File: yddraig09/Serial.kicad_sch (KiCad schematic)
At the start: 22 parts, among them J7 Serial 1, J8 Serial 2, Q2 2N4403, Q3 2N4403, U37 SC26C92C1A, U38 MAX208, Y4 3.6864Mhz

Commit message: Updated yddraig09 silkscreen
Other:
- title: Y Ddraig Fechan -> Y Ddraig Fach
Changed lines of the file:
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@@
   (paper "A4")
   (title_block
-    (title "Y Ddraig Fechan")
+    (title "Y Ddraig Fach")
     (company "Stephen Moody")
   )

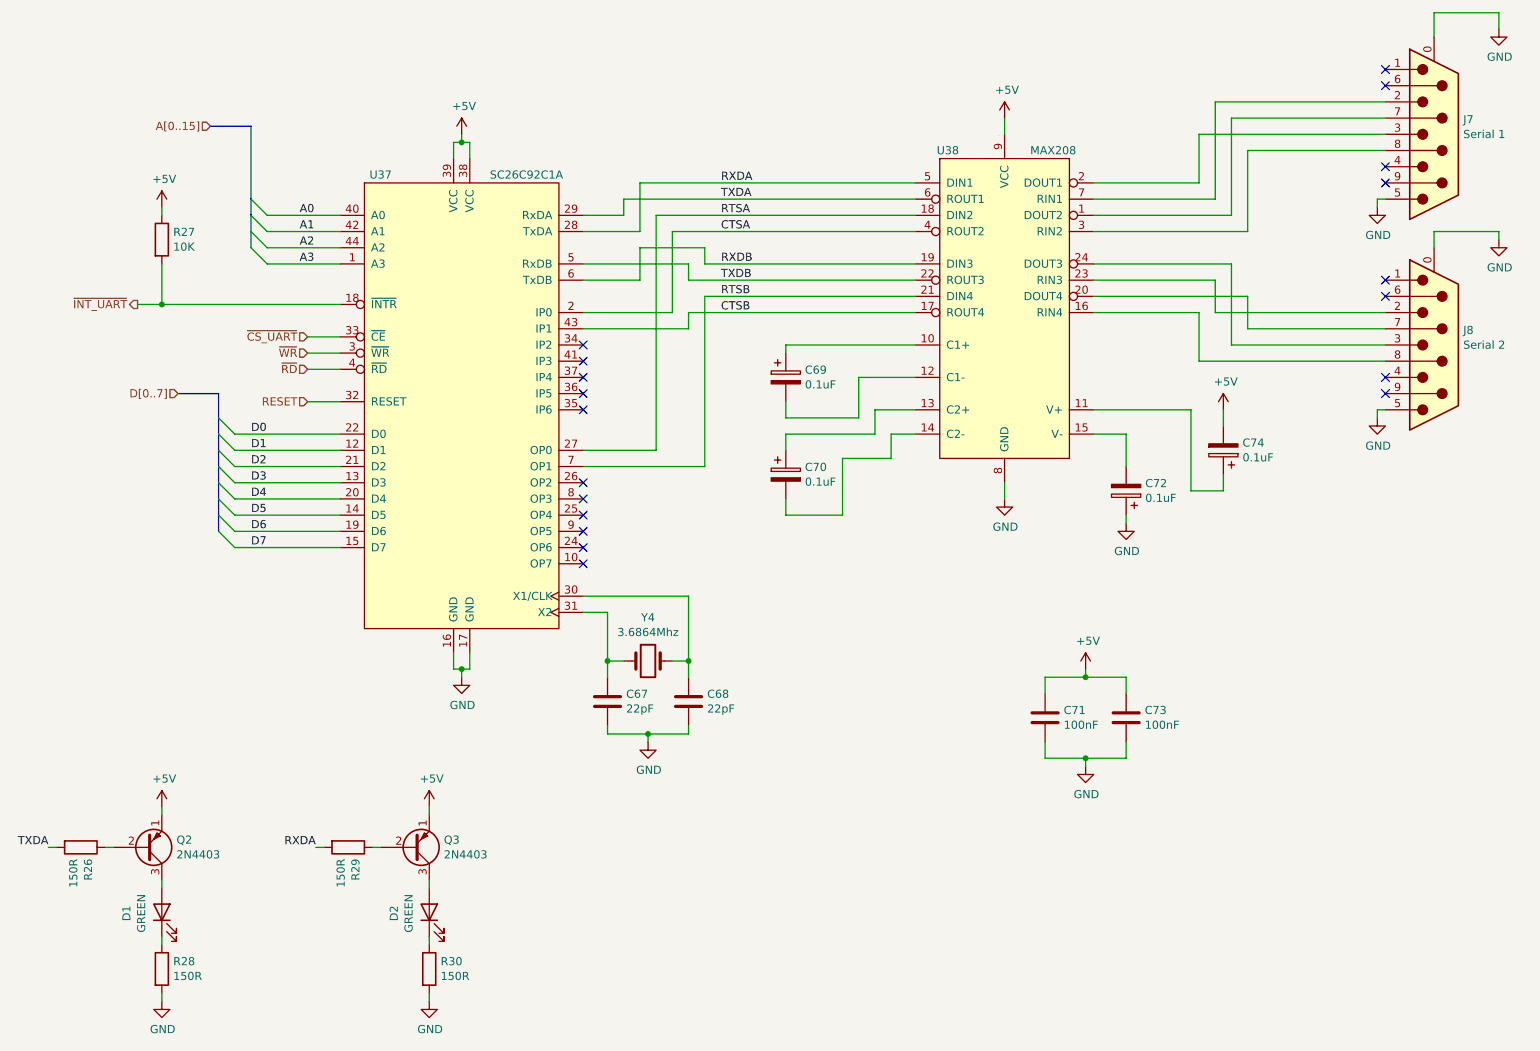
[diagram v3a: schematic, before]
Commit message: Small updates to 6809 and 030 board, remove old files
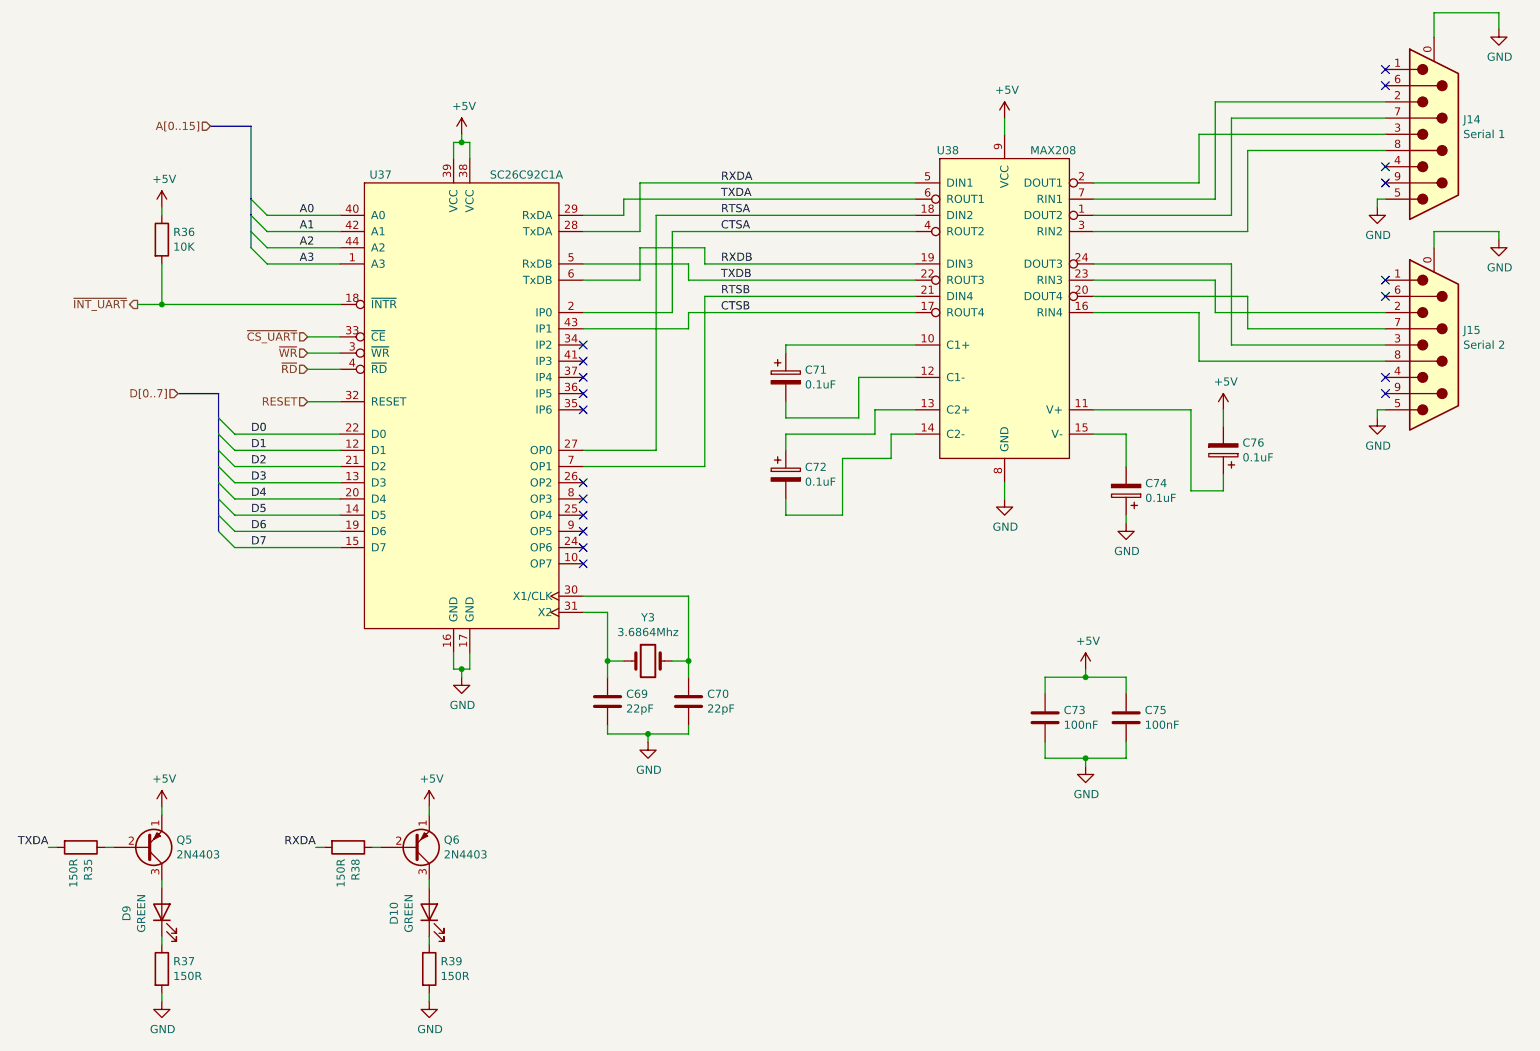
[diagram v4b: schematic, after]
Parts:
- J14: renamed from J7; symbol Connector:DB9_Male_MountingHoles -> Connector:DE9_Plug_MountingHoles
- J15: renamed from J8; symbol Connector:DB9_Male_MountingHoles -> Connector:DE9_Plug_MountingHoles
- renumbered C67 to C69, C68 to C70, C69 to C71, C70 to C72, C71 to C73, C72 to C74, C73 to C75, C74 to C76, D2 to D10, D1 to D9, Q2 to Q5, Q3 to Q6, R26 to R35, R27 to R36, R28 to R37, R29 to R38, R30 to R39, Y4 to Y3

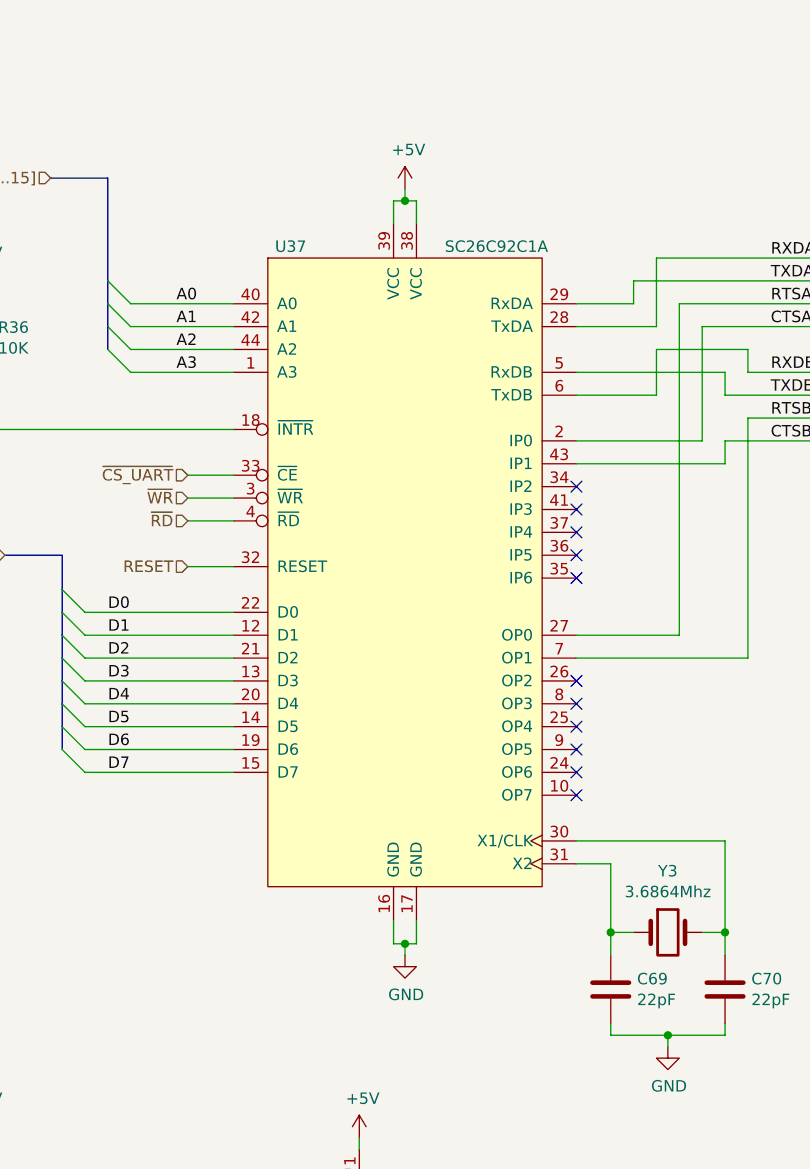
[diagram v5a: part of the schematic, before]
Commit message: Fix the serial port on yddraig09
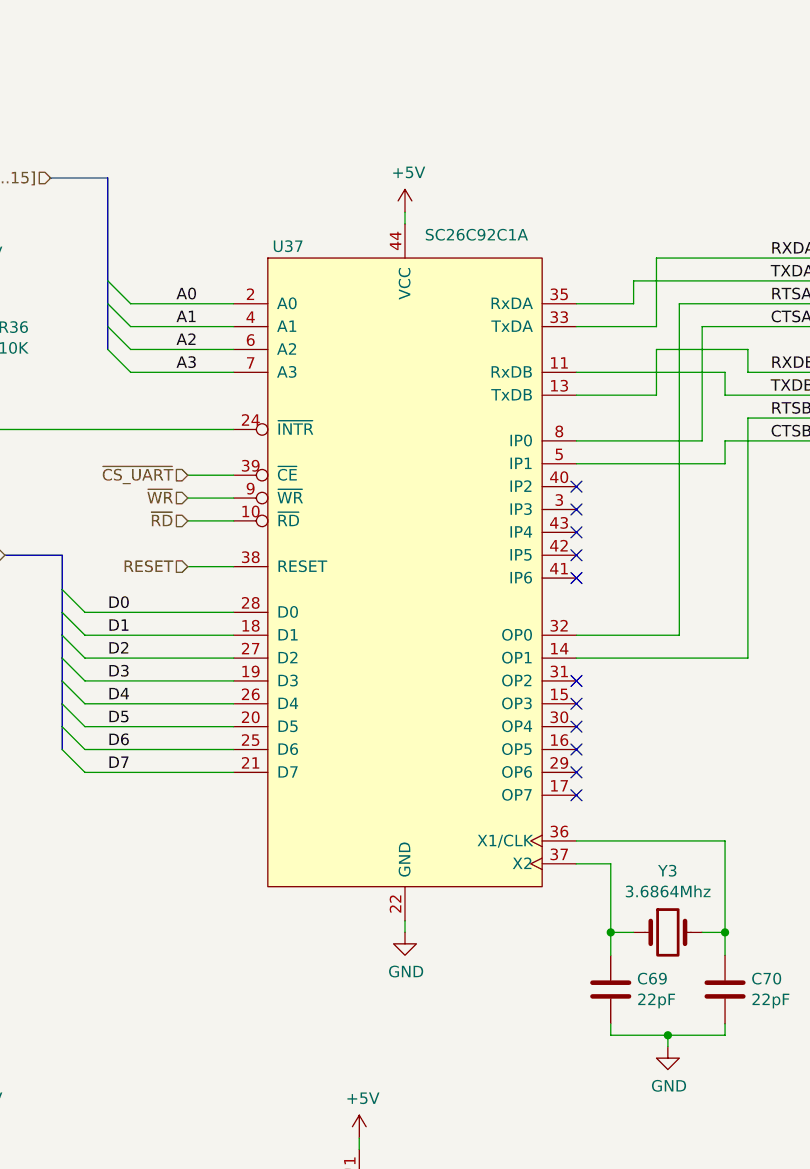
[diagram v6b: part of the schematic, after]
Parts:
- removed U37: SC26C92C1A, Package_LCC:PLCC-44_THT-Socket, symbol Ddraig:SC26C92C1A
- added U37: SC26C92C1A, Package_LCC:PLCC-44_THT-Socket, symbol Ddraig:SC26C92C1A_PLCC
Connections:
- net +5V: now also U37.44 (VCC)
- net A0: now also U37.2 (A0)
- net A1: now also U37.4 (A1)
- net A2: now also U37.6 (A2)
- net A3: now also U37.7 (A3)
- net CTSA: now also U37.8 (IP0)
- net CTSB: now also U37.5 (IP1)
- net D0: now also U37.28 (D0)
- net D1: now also U37.18 (D1)
- net D2: now also U37.27 (D2)
- net D3: now also U37.19 (D3)
- net D4: now also U37.26 (D4)
- net D5: now also U37.20 (D5)
- net D6: now also U37.25 (D6)
- net D7: now also U37.21 (D7)
- net GND: now also U37.22 (GND)
- net RESET: now also U37.38 (RESET)
- net RTSA: now also U37.32 (OP0)
- net RTSB: now also U37.14 (OP1)
- net RXDA: now also U37.33 (TxDA)
- net RXDB: now also U37.13 (TxDB)
- net TXDA: now also U37.35 (RxDA)
- net TXDB: now also U37.11 (RxDB)
- net ~{CS_UART}: now also U37.39 (~{CE})
- net ~{INT_UART}: now also U37.24 (~{INTR})
- net ~{RD}: now also U37.10 (~{RD})
- net ~{WR}: now also U37.9 (~{WR})
- net at C69.1, Y3.1: now also U37.37 (X2)
- net at C70.1, Y3.2: now also U37.36 (X1/CLK)
